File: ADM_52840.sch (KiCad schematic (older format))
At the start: 41 parts, among them J1 JST, J3 Conn_01x16_Male, J4 Conn_01x20_Male, J5 JTAG, P1 USB_micro_B, Q1 DMP2045U, SW1 BTN1, SW2 BTN2, SW3 RESET, U1 HolyIOT_NRF52840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

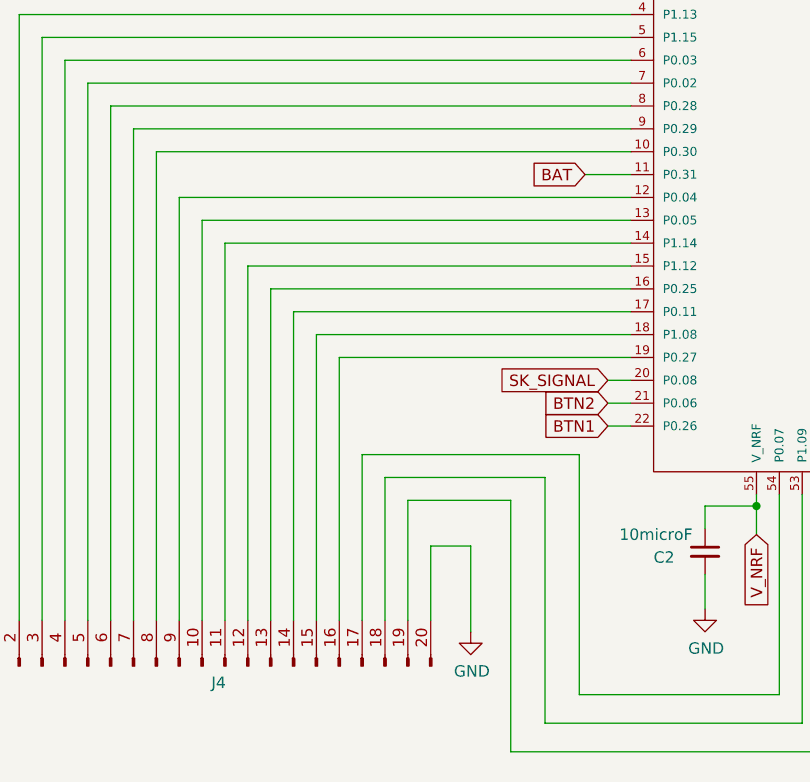
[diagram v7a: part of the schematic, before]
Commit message: PCB Routing
Trying to fit everything now that we have a goal
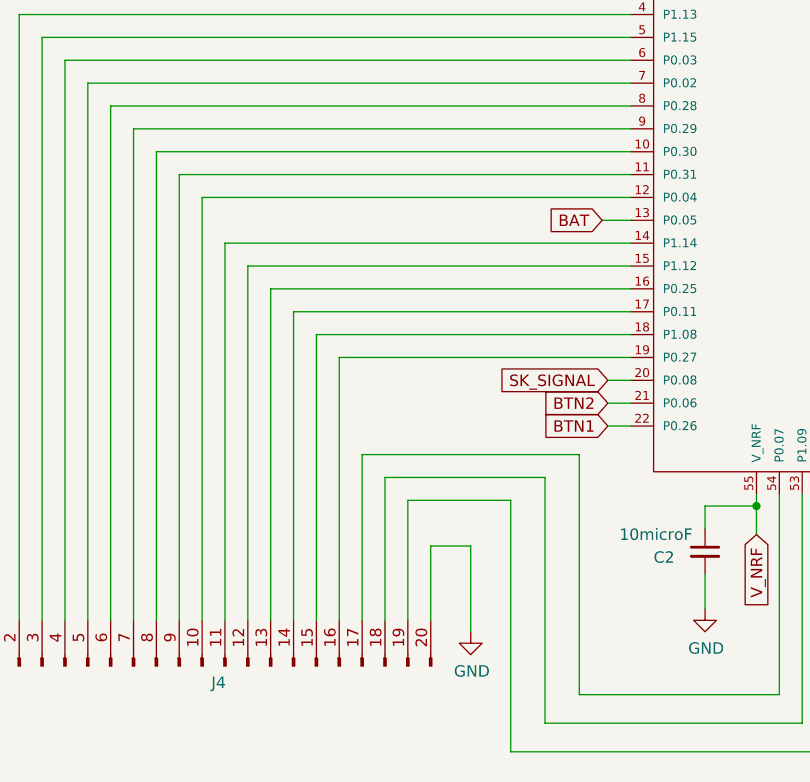
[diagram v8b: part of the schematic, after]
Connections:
- net BAT: now also U1.13 (P0.05); no longer U1.11 (P0.31)
- net at J4.9 (Pin_9): now also U1.11 (P0.31); no longer U1.12 (P0.04)
- net at J4.10 (Pin_10): now also U1.12 (P0.04); no longer U1.13 (P0.05)
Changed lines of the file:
@@
 Text GLabel 7075 5300 1    50   Input ~ 0
 VBAT
-Text GLabel 3500 1800 0    50   Input ~ 0
+Text GLabel 3575 2000 0    50   Input ~ 0
 BAT
 Wire Wire Line
@@
 $EndComp
 Wire Wire Line
-	3700 1800 3500 1800
-Wire Wire Line
 	7550 2900 7550 2525
 Wire Wire Line
@@
 	3600 2900 3700 2900
 Wire Wire Line
-	3700 2000 1825 2000
-Wire Wire Line
-	1825 2000 1825 3750
-Wire Wire Line
-	3700 1900 1725 1900
-Wire Wire Line
-	1725 1900 1725 3750
-Wire Wire Line
 	3700 1700 1625 1700
 Wire Wire Line
@@
 Text GLabel 4675 5525 2    50   Input ~ 0
 BTN1
+Wire Wire Line
+	3575 2000 3700 2000
+Wire Wire Line
+	3700 1800 1725 1800
+Wire Wire Line
+	1725 1800 1725 3750
+Wire Wire Line
+	3700 1900 1825 1900
+Wire Wire Line
+	1825 1900 1825 3750
 $EndSCHEMATC
